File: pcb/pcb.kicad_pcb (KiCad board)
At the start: 2 copper layers, 48 x 60 mm, 40 parts, among them J1 USB_C_Receptacle_USB2.0_14P, J3 LCD Data, J4 LCD CTRL, J5 MOISTURE, J6 HC-05, J7 DEBUG, J9 USART3 TX, SW1 PWR SWITCH, U1 TLV62569DBV, U2 STM32F446RETx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

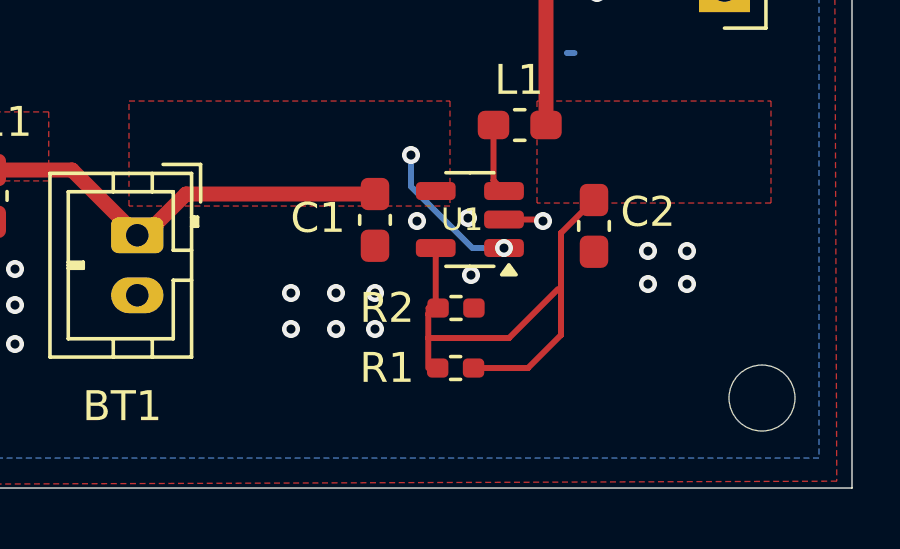
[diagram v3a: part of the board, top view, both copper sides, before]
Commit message: change buck divider resistors
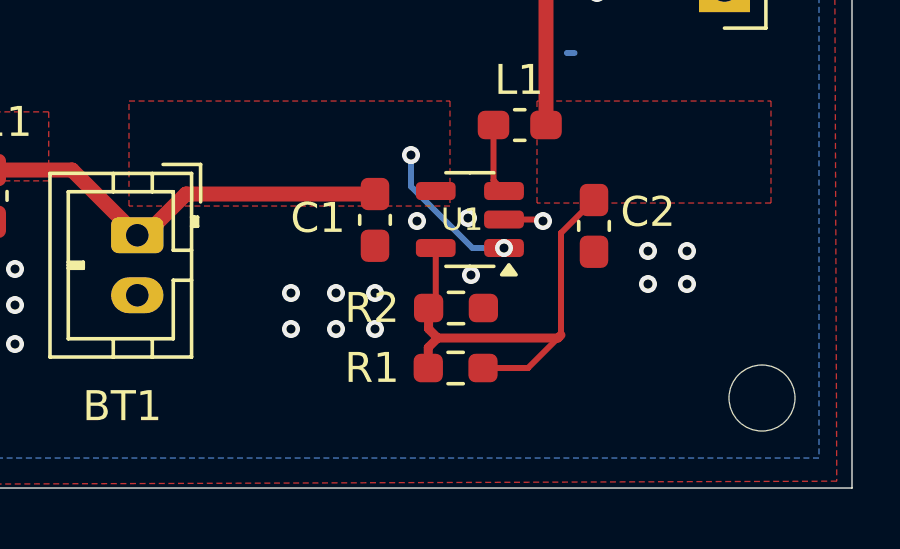
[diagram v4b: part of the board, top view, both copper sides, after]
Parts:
- R1: value 450k -> 453k; footprint Resistor_SMD:R_0402_1005Metric_Pad0.72x0.64mm_HandSolder -> Resistor_SMD:R_0603_1608Metric_Pad0.98x0.95mm_HandSolder
- R2: footprint Resistor_SMD:R_0402_1005Metric_Pad0.72x0.64mm_HandSolder -> Resistor_SMD:R_0603_1608Metric_Pad0.98x0.95mm_HandSolder
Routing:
- net +3.3V: track 142.9 -> 142.0 mm
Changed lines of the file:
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@@
 		)
 	)
-	(footprint "Resistor_SMD:R_0402_1005Metric_Pad0.72x0.64mm_HandSolder"
+	(footprint "Resistor_SMD:R_0603_1608Metric_Pad0.98x0.95mm_HandSolder"
 		(layer "F.Cu")
 		(at 98.7875 95.5 180)
-		(descr "Resistor SMD 0402 (1005 Metric), square (rectangular) end terminal, IPC-7351 nominal with elongated pad for handsoldering. (Body size source: IPC-SM-782 page 72, https://www.pcb-3d.com/wordpress/wp-content/uploads/ipc-sm-782a_amendment_1_and_2.pdf), generated with kicad-footprint-generator")
+		(descr "Resistor SMD 0603 (1608 Metric), square (rectangular) end terminal, IPC-7351 nominal with elongated pad for handsoldering. (Body size source: IPC-SM-782 page 72, https://www.pcb-3d.com/wordpress/wp-content/uploads/ipc-sm-782a_amendment_1_and_2.pdf), generated with kicad-footprint-generator")
 		(tags "resistor handsolder")
 		(property "Reference" "R1"
-			(at 2.2875 0 180)
+			(at 2.7875 0 180)
 			(layer "F.SilkS")
 			(effects
@@
 			)
 		)
-		(property "Value" "450k"
-			(at 0 1.17 180)
+		(property "Value" "453k"
+			(at 0 1.43 180)
 			(layer "F.Fab")
 			(effects
@@
 		(attr smd)
 		(fp_line
-			(start -0.167621 0.38)
-			(end 0.167621 0.38)
+			(start -0.254724 0.5225)
+			(end 0.254724 0.5225)
 			(stroke
 				(width 0.12)
@@
 		)
 		(fp_line
-			(start -0.167621 -0.38)
-			(end 0.167621 -0.38)
+			(start -0.254724 -0.5225)
+			(end 0.254724 -0.5225)
 			(stroke
 				(width 0.12)
@@
 		)
 		(fp_line
-			(start 1.11 0.47)
-			(end -1.11 0.47)
+			(start 1.65 0.73)
+			(end -1.65 0.73)
 			(stroke
 				(width 0.05)
@@
 		)
 		(fp_line
-			(start 1.11 -0.47)
-			(end 1.11 0.47)
+			(start 1.65 -0.73)
+			(end 1.65 0.73)
 			(stroke
 				(width 0.05)
@@
 		)
 		(fp_line
-			(start -1.11 0.47)
-			(end -1.11 -0.47)
+			(start -1.65 0.73)
+			(end -1.65 -0.73)
 			(stroke
 				(width 0.05)
@@
 		)
 		(fp_line
-			(start -1.11 -0.47)
-			(end 1.11 -0.47)
+			(start -1.65 -0.73)
+			(end 1.65 -0.73)
 			(stroke
 				(width 0.05)
@@
 		)
 		(fp_line
-			(start 0.525 0.27)
-			(end -0.525 0.27)
+			(start 0.8 0.4125)
+			(end -0.8 0.4125)
 			(stroke
 				(width 0.1)
@@
 		)
 		(fp_line
-			(start 0.525 -0.27)
-			(end 0.525 0.27)
+			(start 0.8 -0.4125)
+			(end 0.8 0.4125)
 			(stroke
 				(width 0.1)
@@
 		)
 		(fp_line
-			(start -0.525 0.27)
-			(end -0.525 -0.27)
+			(start -0.8 0.4125)
+			(end -0.8 -0.4125)
 			(stroke
 				(width 0.1)
@@
 		)
 		(fp_line
-			(start -0.525 -0.27)
-			(end 0.525 -0.27)
+			(start -0.8 -0.4125)
+			(end 0.8 -0.4125)
 			(stroke
 				(width 0.1)
@@
 			(effects
 				(font
-					(size 0.26 0.26)
-					(thickness 0.04)
+					(size 0.4 0.4)
+					(thickness 0.06)
 				)
 			)
 		)
 		(pad "1" smd roundrect
-			(at -0.5975 0 180)
-			(size 0.715 0.64)
+			(at -0.9125 0 180)
+			(size 0.975 0.95)
 			(layers "F.Cu" "F.Mask" "F.Paste")
 			(roundrect_rratio 0.25)
@@
 		)
 		(pad "2" smd roundrect
-			(at 0.5975 0 180)
-			(size 0.715 0.64)
+			(at 0.9125 0 180)
+			(size 0.975 0.95)
 			(layers "F.Cu" "F.Mask" "F.Paste")
 			(roundrect_rratio 0.25)
@@
 		)
 		(embedded_fonts no)
-		(model "${KICAD9_3DMODEL_DIR}/Resistor_SMD.3dshapes/R_0402_1005Metric.step"
+		(model "${KICAD9_3DMODEL_DIR}/Resistor_SMD.3dshapes/R_0603_1608Metric.step"
 			(offset
 				(xyz 0 0 0)
@@
 		(embedded_fonts no)
 	)
-	(footprint "Resistor_SMD:R_0402_1005Metric_Pad0.72x0.64mm_HandSolder"
+	(footprint "Resistor_SMD:R_0603_1608Metric_Pad0.98x0.95mm_HandSolder"
 		(layer "F.Cu")
 		(at 98.8 93.5)
-		(descr "Resistor SMD 0402 (1005 Metric), square (rectangular) end terminal, IPC-7351 nominal with elongated pad for handsoldering. (Body size source: IPC-SM-782 page 72, https://www.pcb-3d.com/wordpress/wp-content/uploads/ipc-sm-782a_amendment_1_and_2.pdf), generated with kicad-footprint-generator")
+		(descr "Resistor SMD 0603 (1608 Metric), square (rectangular) end terminal, IPC-7351 nominal with elongated pad for handsoldering. (Body size source: IPC-SM-782 page 72, https://www.pcb-3d.com/wordpress/wp-content/uploads/ipc-sm-782a_amendment_1_and_2.pdf), generated with kicad-footprint-generator")
 		(tags "resistor handsolder")
 		(property "Reference" "R2"
-			(at -2.3 0 0)
+			(at -2.8 0 0)
 			(layer "F.SilkS")
 			(effects
@@
 		)
 		(property "Value" "100k"
-			(at 0 1.17 0)
+			(at 0 1.43 0)
 			(layer "F.Fab")
 			(effects
@@
 		(attr smd)
 		(fp_line
-			(start -0.167621 -0.38)
-			(end 0.167621 -0.38)
+			(start -0.254724 -0.5225)
+			(end 0.254724 -0.5225)
 			(stroke
 				(width 0.12)
@@
 		)
 		(fp_line
-			(start -0.167621 0.38)
-			(end 0.167621 0.38)
+			(start -0.254724 0.5225)
+			(end 0.254724 0.5225)
 			(stroke
 				(width 0.12)
@@
 		)
 		(fp_line
-			(start -1.11 -0.47)
-			(end 1.11 -0.47)
+			(start -1.65 -0.73)
+			(end 1.65 -0.73)
 			(stroke
 				(width 0.05)
@@
 		)
 		(fp_line
-			(start -1.11 0.47)
-			(end -1.11 -0.47)
+			(start -1.65 0.73)
+			(end -1.65 -0.73)
 			(stroke
 				(width 0.05)
@@
 		)
 		(fp_line
-			(start 1.11 -0.47)
-			(end 1.11 0.47)
+			(start 1.65 -0.73)
+			(end 1.65 0.73)
 			(stroke
 				(width 0.05)
@@
 		)
 		(fp_line
-			(start 1.11 0.47)
-			(end -1.11 0.47)
+			(start 1.65 0.73)
+			(end -1.65 0.73)
 			(stroke
 				(width 0.05)
@@
 		)
 		(fp_line
-			(start -0.525 -0.27)
-			(end 0.525 -0.27)
+			(start -0.8 -0.4125)
+			(end 0.8 -0.4125)
 			(stroke
 				(width 0.1)
@@
 		)
 		(fp_line
-			(start -0.525 0.27)
-			(end -0.525 -0.27)
+			(start -0.8 0.4125)
+			(end -0.8 -0.4125)
 			(stroke
 				(width 0.1)
@@
 		)
 		(fp_line
-			(start 0.525 -0.27)
-			(end 0.525 0.27)
+			(start 0.8 -0.4125)
+			(end 0.8 0.4125)
 			(stroke
 				(width 0.1)
@@
 		)
 		(fp_line
-			(start 0.525 0.27)
-			(end -0.525 0.27)
+			(start 0.8 0.4125)
+			(end -0.8 0.4125)
 			(stroke
 				(width 0.1)
@@
 			(effects
 				(font
-					(size 0.26 0.26)
-					(thickness 0.04)
+					(size 0.4 0.4)
+					(thickness 0.06)
 				)
 			)
 		)
 		(pad "1" smd roundrect
-			(at -0.5975 0)
-			(size 0.715 0.64)
+			(at -0.9125 0)
+			(size 0.975 0.95)
 			(layers "F.Cu" "F.Mask" "F.Paste")
 			(roundrect_rratio 0.25)
@@
 		)
 		(pad "2" smd roundrect
-			(at 0.5975 0)
-			(size 0.715 0.64)
+			(at 0.9125 0)
+			(size 0.975 0.95)
 			(layers "F.Cu" "F.Mask" "F.Paste")
 			(roundrect_rratio 0.25)
@@
 		)
 		(embedded_fonts no)
-		(model "${KICAD9_3DMODEL_DIR}/Resistor_SMD.3dshapes/R_0402_1005Metric.step"
+		(model "${KICAD9_3DMODEL_DIR}/Resistor_SMD.3dshapes/R_0603_1608Metric.step"
 			(offset
 				(xyz 0 0 0)
@@
 	)
 	(segment
-		(start 100.568134 94.5)
-		(end 102.2 92.868134)
-		(width 0.2)
-		(layer "F.Cu")
-		(net 3)
-	)
-	(segment
 		(start 77.75 64.85)
 		(end 77.1625 64.2625)
@@
 	)
 	(segment
+		(start 98.19 94.5)
+		(end 97.875 94.815)
+		(width 0.3)
+		(layer "F.Cu")
+		(net 3)
+	)
+	(segment
 		(start 101.2 95.5)
 		(end 102.3 94.4)
@@
 	)
 	(segment
-		(start 97.875 94.5)
-		(end 100.568134 94.5)
-		(width 0.2)
-		(layer "F.Cu")
-		(net 3)
-	)
-	(segment
 		(start 97.535 73.925)
 		(end 96.5 74.96)
@@
 	)
 	(segment
-		(start 97.875 94.5)
-		(end 97.875 95.5)
-		(width 0.2)
-		(layer "F.Cu")
-		(net 3)
-	)
-	(segment
 		(start 80.075 59.425)
 		(end 81.325 59.425)
@@
 	)
 	(segment
-		(start 97.8875 93.5)
-		(end 97.8875 93.6875)
-		(width 0.2)
-		(layer "F.Cu")
-		(net 3)
-	)
-	(segment
 		(start 89.223943 60.726)
 		(end 83.901 60.726)
@@
 	)
 	(segment
+		(start 97.875 94.815)
+		(end 97.875 95.5)
+		(width 0.3)
+		(layer "F.Cu")
+		(net 3)
+	)
+	(segment
+		(start 98.19 94.5)
+		(end 97.8875 94.1975)
+		(width 0.3)
+		(layer "F.Cu")
+		(net 3)
+	)
+	(segment
 		(start 78.8625 58.2125)
 		(end 80.075 59.425)
@@
 	)
 	(segment
-		(start 98.125 93.2625)
-		(end 97.8875 93.5)
-		(width 0.2)
+		(start 83.901 60.651)
+		(end 82 58.75)
+		(width 0.4)
 		(layer "F.Cu")
 		(net 3)
 	)
 	(segment
-		(start 83.901 60.651)
-		(end 82 58.75)
-		(width 0.4)
+		(start 102.3 94.4)
+		(end 102.3 92)
+		(width 0.2)
 		(layer "F.Cu")
 		(net 3)
@@
 	)
 	(segment
-		(start 97.875 93.7)
-		(end 97.875 94.5)
-		(width 0.2)
+		(start 97.8875 94.1975)
+		(end 97.8875 93.5)
+		(width 0.3)
 		(layer "F.Cu")
 		(net 3)
@@
 	)
 	(segment
+		(start 98.19 93.5125)
+		(end 98.2025 93.5)
+		(width 0.2)
+		(layer "F.Cu")
+		(net 3)
+	)
+	(segment
 		(start 83.399 62.909824)
 		(end 83.399 61.153)
@@
 	)
 	(segment
+		(start 98.19 94.5)
+		(end 102.2 94.5)
+		(width 0.3)
+		(layer "F.Cu")
+		(net 3)
+	)
+	(segment
 		(start 102.3 91)
 		(end 103.4 89.9)
@@
 	)
 	(segment
-		(start 97.8875 93.6875)
-		(end 97.875 93.7)
-		(width 0.2)
-		(layer "F.Cu")
-		(net 3)
-	)
-	(segment
 		(start 90.8875 69.3475)
 		(end 96.5 74.96)
@@
 	)
 	(segment
+		(start 102.2 94.5)
+		(end 102.3 94.4)
+		(width 0.3)
+		(layer "F.Cu")
+		(net 3)
+	)
+	(segment
 		(start 80.075 65.425)
 		(end 80.883824 65.425)
@@
 	)
 	(segment
-		(start 102.3 94.4)
+		(start 102.3 92)
 		(end 102.3 91)
 		(width 0.2)

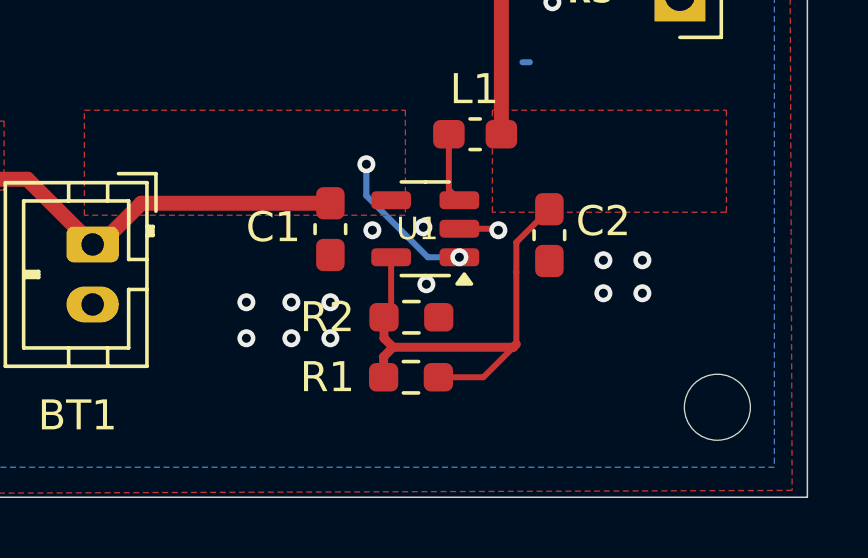
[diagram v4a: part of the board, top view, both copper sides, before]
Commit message: fix buck converter trace and add gerbers
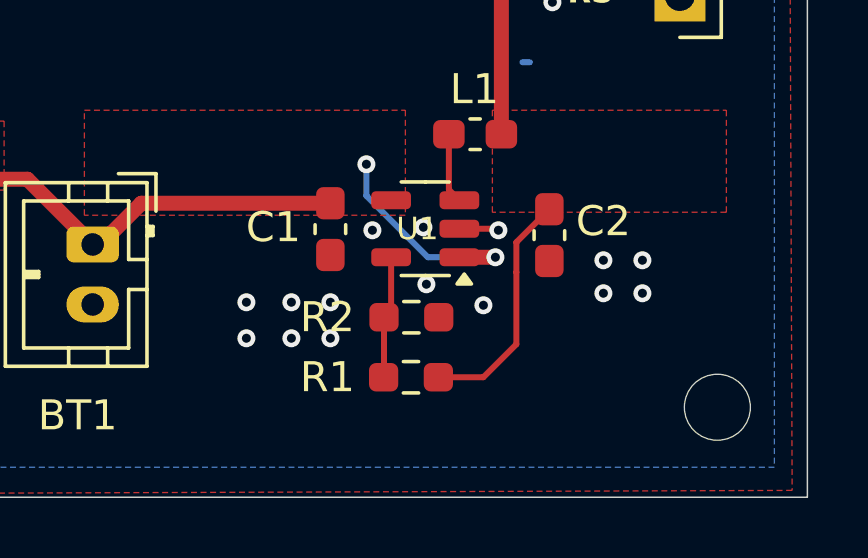
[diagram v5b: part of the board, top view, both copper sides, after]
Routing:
- net +3.3V: track 142.0 -> 137.6 mm
- net +3.7V: track 21.7 -> 24.1 mm
- net GND: vias 65 -> 66
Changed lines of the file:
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@@
 			(drillshape 0)
 			(scaleselection 1)
-			(outputdirectory "gerber/drill/")
+			(outputdirectory "gerber/")
 		)
 	)
@@
 	)
 	(segment
+		(start 101.6 91.5)
+		(end 100.4 91.5)
+		(width 0.5)
+		(layer "F.Cu")
+		(net 1)
+	)
+	(segment
 		(start 88.426 91.074)
 		(end 89.8 89.7)
@@
 	)
 	(via
-		(at 100.4 91.5)
+		(at 97.3 88.4)
 		(size 0.6)
 		(drill 0.3)
 		(layers "F.Cu" "B.Cu")
+		(free yes)
 		(net 1)
 	)
 	(via
-		(at 97.3 88.4)
+		(at 101.6 91.5)
 		(size 0.6)
 		(drill 0.3)
@@
 	)
 	(segment
-		(start 97.3 88.4)
-		(end 97.3 89.449943)
+		(start 99.350057 91.5)
+		(end 101.6 91.5)
 		(width 0.2)
 		(layer "B.Cu")
@@
 	)
 	(segment
-		(start 99.350057 91.5)
-		(end 100.4 91.5)
+		(start 97.3 89.449943)
+		(end 99.350057 91.5)
 		(width 0.2)
 		(layer "B.Cu")
@@
 	)
 	(segment
-		(start 97.3 89.449943)
-		(end 99.350057 91.5)
+		(start 97.3 88.4)
+		(end 97.3 89.449943)
 		(width 0.2)
 		(layer "B.Cu")
@@
 	)
 	(via
+		(at 101.2 93.1)
+		(size 0.6)
+		(drill 0.3)
+		(layers "F.Cu" "B.Cu")
+		(free yes)
+		(net 2)
+	)
+	(via
 		(at 105.6 52.4)
 		(size 0.6)
@@
 	)
 	(segment
-		(start 98.19 94.5)
-		(end 97.875 94.815)
-		(width 0.3)
+		(start 101.2 95.5)
+		(end 102.3 94.4)
+		(width 0.2)
 		(layer "F.Cu")
 		(net 3)
 	)
 	(segment
-		(start 101.2 95.5)
-		(end 102.3 94.4)
+		(start 97.8875 95.4875)
+		(end 97.875 95.5)
 		(width 0.2)
 		(layer "F.Cu")
@@
 	)
 	(segment
-		(start 97.875 94.815)
-		(end 97.875 95.5)
-		(width 0.3)
-		(layer "F.Cu")
-		(net 3)
-	)
-	(segment
-		(start 98.19 94.5)
-		(end 97.8875 94.1975)
-		(width 0.3)
-		(layer "F.Cu")
-		(net 3)
-	)
-	(segment
 		(start 78.8625 58.2125)
 		(end 80.075 59.425)
@@
 	)
 	(segment
-		(start 97.8875 94.1975)
-		(end 97.8875 93.5)
-		(width 0.3)
-		(layer "F.Cu")
-		(net 3)
-	)
-	(segment
 		(start 101.275 73.925)
 		(end 97.535 73.925)
@@
 	)
 	(segment
-		(start 98.19 94.5)
-		(end 102.2 94.5)
-		(width 0.3)
-		(layer "F.Cu")
-		(net 3)
-	)
-	(segment
 		(start 102.3 91)
 		(end 103.4 89.9)
@@
 	)
 	(segment
-		(start 90.8875 69.3475)
-		(end 96.5 74.96)
+		(start 97.8875 93.5)
+		(end 97.8875 95.4875)
 		(width 0.2)
 		(layer "F.Cu")
@@
 	)
 	(segment
-		(start 100.925 73.925)
-		(end 100 73)
+		(start 90.8875 69.3475)
+		(end 96.5 74.96)
 		(width 0.2)
 		(layer "F.Cu")
@@
 	)
 	(segment
-		(start 102.2 94.5)
-		(end 102.3 94.4)
-		(width 0.3)
+		(start 100.925 73.925)
+		(end 100 73)
+		(width 0.2)
 		(layer "F.Cu")
 		(net 3)
